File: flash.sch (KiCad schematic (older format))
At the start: 13 parts, among them J1 USB_B_Micro, Q1 PN2222A, Q2 PN2222A, U1 CP2102N-A01-GQFN24

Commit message: Add first iteration of PCB design
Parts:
- added J2: Conn_01x05, Pin_Headers:Pin_Header_Straight_1x05_Pitch2.54mm, symbol Connector_Generic:Conn_01x05
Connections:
- net EN: now also J2.1 (Pin_1)
- net GND: now also J2.5 (Pin_5)
- net GPIO0: now also J2.4 (Pin_4)
- net RX: now also J2.3 (Pin_3)
- net TX: now also J2.2 (Pin_2)
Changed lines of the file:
@@
 Wire Wire Line
 	7800 3700 8300 3700
+$Comp
+L Connector_Generic:Conn_01x05 J2
+U 1 1 5CD3182A
+P 9750 2650
+F 0 "J2" H 9830 2692 50  0000 L CNN
+F 1 "Conn_01x05" H 9830 2601 50  0000 L CNN
+F 2 "Pin_Headers:Pin_Header_Straight_1x05_Pitch2.54mm" H 9750 2650 50  0001 C CNN
+F 3 "~" H 9750 2650 50  0001 C CNN
+	1    9750 2650
+	1    0    0    -1
+$EndComp
+Wire Wire Line
+	9550 2850 9350 2850
+Wire Wire Line
+	9350 2850 9350 3050
+$Comp
+L power:GND #PWR07
+U 1 1 5CD34B89
+P 9350 3050
+F 0 "#PWR07" H 9350 2800 50  0001 C CNN
+F 1 "GND" H 9355 2877 50  0000 C CNN
+F 2 "" H 9350 3050 50  0001 C CNN
+F 3 "" H 9350 3050 50  0001 C CNN
+	1    9350 3050
+	1    0    0    -1
+$EndComp
+Wire Wire Line
+	9550 2750 9350 2750
+Text Label 9350 2750 2    50   ~ 0
+GPIO0
+Wire Wire Line
+	9550 2650 9350 2650
+Text Label 9350 2650 2    50   ~ 0
+RX
+Wire Wire Line
+	9550 2550 9350 2550
+Text Label 9350 2550 2    50   ~ 0
+TX
+Wire Wire Line
+	9550 2450 9350 2450
+Text Label 9350 2450 2    50   ~ 0
+EN
 $EndSCHEMATC

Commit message: Finish PCB
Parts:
- U1: footprint digikey-footprints:QFN-24-1EP_4x4mm -> Housings_DFN_QFN:QFN-24-1EP_4x4mm_Pitch0.5mm
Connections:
- net at R1.1, U1.5 (VIO): now also C1.1, C2.1, U1.6 (VDD)
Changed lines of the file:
@@
 F 0 "U1" H 5800 4581 50  0000 C CNN
 F 1 "CP2102N-A01-GQFN24" H 5800 4490 50  0000 C CNN
-F 2 "digikey-footprints:QFN-24-1EP_4x4mm" H 6250 2700 50  0001 L CNN
+F 2 "Housings_DFN_QFN:QFN-24-1EP_4x4mm_Pitch0.5mm" H 6250 2700 50  0001 L CNN
 F 3 "https://www.silabs.com/documents/public/data-sheets/cp2102n-datasheet.pdf" H 5850 2450 50  0001 C CNN
 	1    5800 3500
@@
 	5800 2600 5800 2150
 Wire Wire Line
-	5800 2150 5500 2150
+	5800 2150 5700 2150
 Wire Wire Line
 	7800 2450 8300 2450
@@
 Text Label 9350 2450 2    50   ~ 0
 EN
+Wire Wire Line
+	5700 2400 5700 2150
+Connection ~ 5700 2400
+Connection ~ 5700 2150
+Wire Wire Line
+	5700 2150 5500 2150
 $EndSCHEMATC

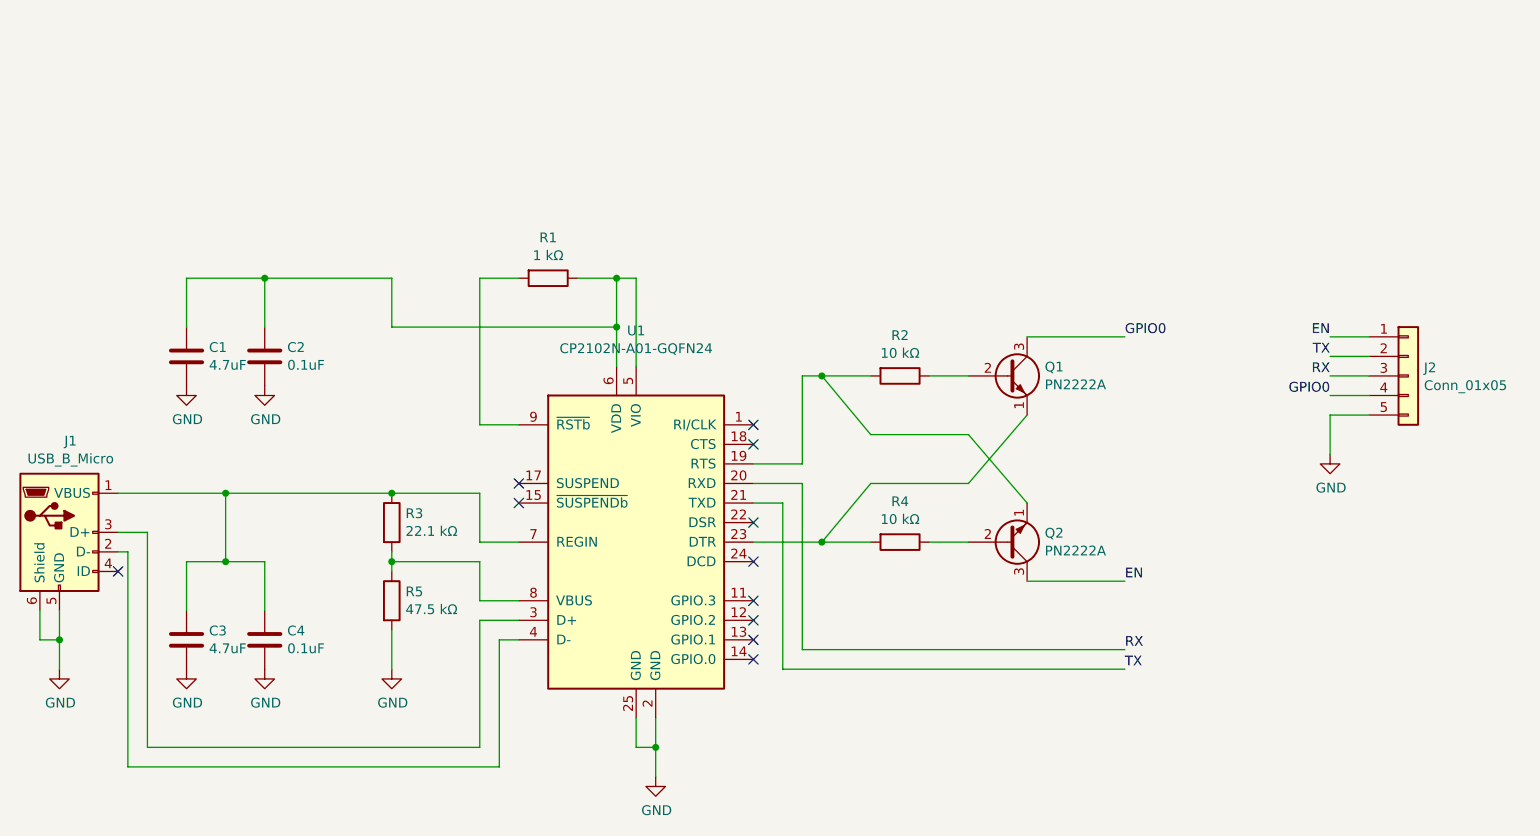
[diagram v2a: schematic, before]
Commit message: Swap RX/TX pins, fix DTR/RTS transistor wiring
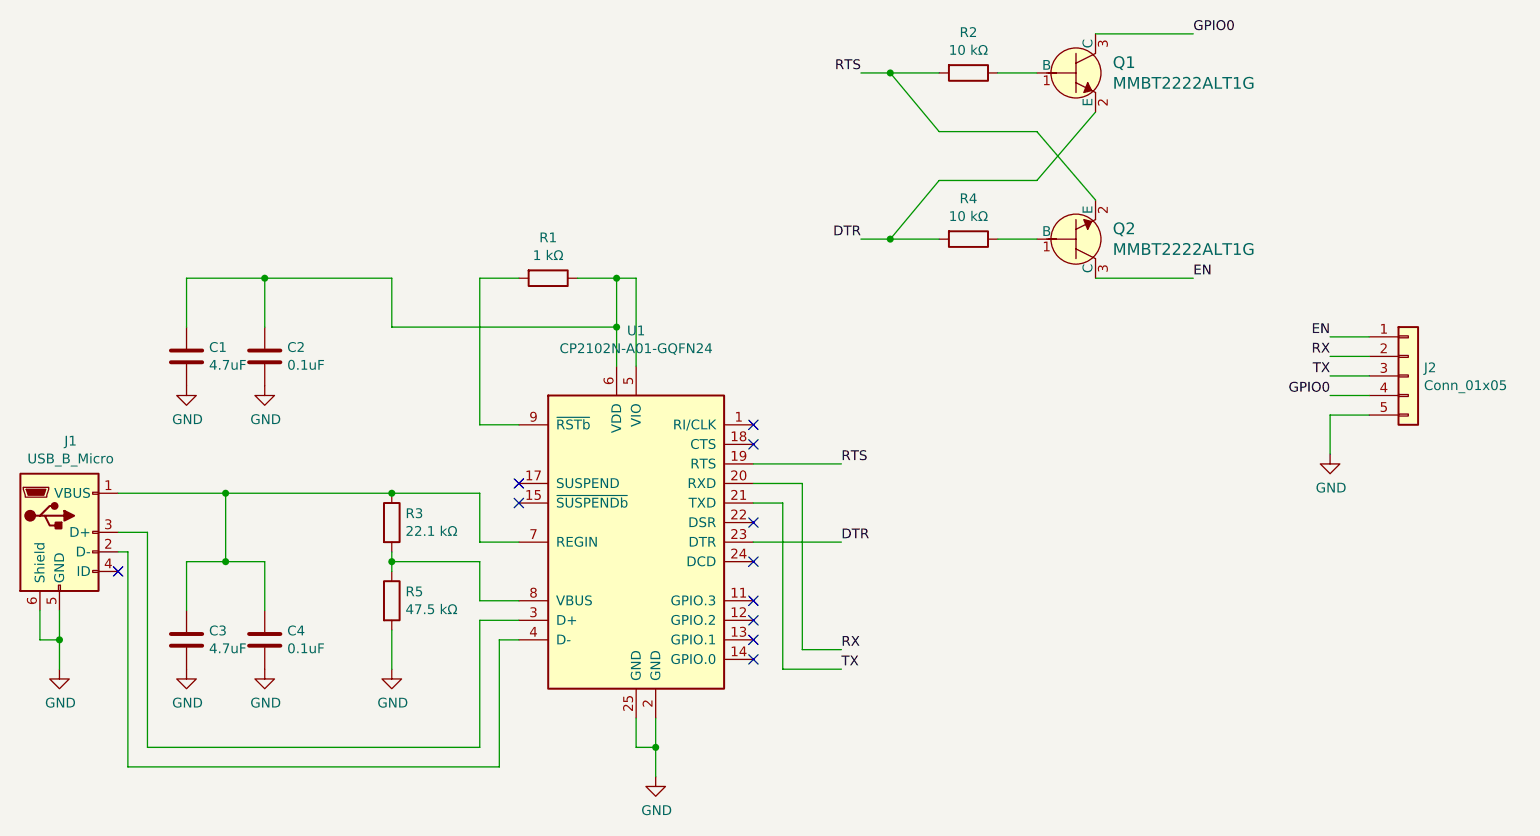
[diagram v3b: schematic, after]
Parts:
- removed Q1, Q2: PN2222A, mmbt2222alt1g:mmbt2222alt1g, symbol Transistor_BJT:PN2222A
- added Q1, Q2: MMBT2222ALT1G, mmbt2222alt1g:mmbt2222alt1g, symbol dk_Transistors-Bipolar-BJT-Single:MMBT2222ALT1G
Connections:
- net EN: now also Q2.3 (C)
- net GPIO0: now also Q1.3 (C)
- net RX: now also J2.2 (Pin_2); no longer J2.3 (Pin_3)
- net TX: now also J2.3 (Pin_3); no longer J2.2 (Pin_2)
- net RTS: now reaches R2.2, U1.19 (RTS)
- net RTS: now also Q2.2 (E)
- net DTR: now reaches R4.2, U1.23 (DTR)
- net DTR: now also Q1.2 (E)
- net at R4.1: now also Q2.1 (B)
- net at R2.1: now also Q1.1 (B)
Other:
- moved on the sheet: R2, R4
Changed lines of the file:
@@
 L Device:R R4
 U 1 1 5CD352C9
-P 7150 3500
-F 0 "R4" V 6943 3500 50  0000 C CNN
-F 1 "10 kΩ" V 7034 3500 50  0000 C CNN
-F 2 "Resistors_SMD:R_0603_HandSoldering" V 7080 3500 50  0001 C CNN
-F 3 "~" H 7150 3500 50  0001 C CNN
-	1    7150 3500
+P 7500 1950
+F 0 "R4" V 7293 1950 50  0000 C CNN
+F 1 "10 kΩ" V 7384 1950 50  0000 C CNN
+F 2 "Resistors_SMD:R_0603_HandSoldering" V 7430 1950 50  0001 C CNN
+F 3 "~" H 7500 1950 50  0001 C CNN
+	1    7500 1950
 	0    1    1    0
 $EndComp
-$Comp
-L Transistor_BJT:PN2222A Q2
-U 1 1 5CD37793
-P 7700 3500
-F 0 "Q2" H 7890 3454 50  0000 L CNN
-F 1 "PN2222A" H 7890 3545 50  0000 L CNN
-F 2 "mmbt2222alt1g:mmbt2222alt1g" H 7900 3425 50  0001 L CIN
-F 3 "http://www.fairchildsemi.com/ds/PN/PN2222A.pdf" H 7700 3500 50  0001 L CNN
-	1    7700 3500
-	1    0    0    1
-$EndComp
-Wire Wire Line
-	7300 3500 7500 3500
+Wire Wire Line
+	7650 1950 7850 1950
 $Comp
 L Device:R R2
 U 1 1 5CD3C513
-P 7150 2650
-F 0 "R2" V 6943 2650 50  0000 C CNN
-F 1 "10 kΩ" V 7034 2650 50  0000 C CNN
-F 2 "Resistors_SMD:R_0603_HandSoldering" V 7080 2650 50  0001 C CNN
-F 3 "~" H 7150 2650 50  0001 C CNN
-	1    7150 2650
+P 7500 1100
+F 0 "R2" V 7293 1100 50  0000 C CNN
+F 1 "10 kΩ" V 7384 1100 50  0000 C CNN
+F 2 "Resistors_SMD:R_0603_HandSoldering" V 7430 1100 50  0001 C CNN
+F 3 "~" H 7500 1100 50  0001 C CNN
+	1    7500 1100
 	0    1    1    0
 $EndComp
-Text Label 8300 3700 0    50   ~ 0
+Text Label 8650 2150 0    50   ~ 0
 EN
-Text Label 8300 2450 0    50   ~ 0
+Text Label 8650 900  0    50   ~ 0
 GPIO0
 Wire Wire Line
 	6550 3300 6550 4150
-Wire Wire Line
-	6550 4150 8300 4150
-Text Label 8300 4150 0    50   ~ 0
+Text Label 6850 4150 0    50   ~ 0
 TX
-$Comp
-L Transistor_BJT:PN2222A Q1
-U 1 1 5CD387D0
-P 7700 2650
-F 0 "Q1" H 7890 2696 50  0000 L CNN
-F 1 "PN2222A" H 7890 2605 50  0000 L CNN
-F 2 "mmbt2222alt1g:mmbt2222alt1g" H 7900 2575 50  0001 L CIN
-F 3 "http://www.fairchildsemi.com/ds/PN/PN2222A.pdf" H 7700 2650 50  0001 L CNN
-	1    7700 2650
-	1    0    0    -1
-$EndComp
-Wire Wire Line
-	7300 2650 7500 2650
-Wire Wire Line
-	6400 3500 6750 3500
-Wire Wire Line
-	6750 3500 7000 3200
-Connection ~ 6750 3500
-Wire Wire Line
-	6750 3500 7000 3500
-Wire Wire Line
-	6750 2650 7000 2650
-Wire Wire Line
-	6750 2650 7000 2950
-Wire Wire Line
-	6400 3100 6650 3100
-Wire Wire Line
-	6650 3100 6650 2650
-Wire Wire Line
-	6650 2650 6750 2650
-Connection ~ 6750 2650
-Wire Wire Line
-	7800 2850 7500 3200
-Wire Wire Line
-	7500 3200 7000 3200
-Wire Wire Line
-	7000 2950 7500 2950
-Wire Wire Line
-	7500 2950 7800 3300
+Wire Wire Line
+	7650 1100 7850 1100
+Wire Wire Line
+	7100 1950 7350 1650
+Wire Wire Line
+	7100 1950 7350 1950
+Wire Wire Line
+	7100 1100 7350 1100
+Wire Wire Line
+	7100 1100 7350 1400
+Wire Wire Line
+	8150 1300 7850 1650
+Wire Wire Line
+	7850 1650 7350 1650
+Wire Wire Line
+	7350 1400 7850 1400
+Wire Wire Line
+	7850 1400 8150 1750
 Wire Wire Line
 	5200 3800 5000 3800
@@
 	5800 2150 5700 2150
 Wire Wire Line
-	7800 2450 8300 2450
+	8150 900  8650 900
 Wire Wire Line
 	6400 3200 6650 3200
 Wire Wire Line
 	6650 3200 6650 4050
-Text Label 8300 4050 0    50   ~ 0
+Text Label 6850 4050 0    50   ~ 0
 RX
 Wire Wire Line
-	6650 4050 8300 4050
-Wire Wire Line
-	7800 3700 8300 3700
+	8150 2150 8650 2150
 $Comp
 L Connector_Generic:Conn_01x05 J2
@@
 Wire Wire Line
 	9550 2650 9350 2650
+Text Label 9350 2550 2    50   ~ 0
+RX
+Wire Wire Line
+	9550 2550 9350 2550
 Text Label 9350 2650 2    50   ~ 0
-RX
-Wire Wire Line
-	9550 2550 9350 2550
-Text Label 9350 2550 2    50   ~ 0
 TX
 Wire Wire Line
@@
 Wire Wire Line
 	5700 2150 5500 2150
+Text Label 6850 3100 0    50   ~ 0
+RTS
+Wire Wire Line
+	6400 3500 6850 3500
+Text Label 6850 3500 0    50   ~ 0
+DTR
+Wire Wire Line
+	6400 3100 6850 3100
+Wire Wire Line
+	7100 1950 6950 1950
+Connection ~ 7100 1950
+Wire Wire Line
+	7100 1100 6950 1100
+Connection ~ 7100 1100
+Text Label 6950 1100 2    50   ~ 0
+RTS
+Text Label 6950 1950 2    50   ~ 0
+DTR
+Wire Wire Line
+	6650 4050 6850 4050
+Wire Wire Line
+	6550 4150 6850 4150
+$Comp
+L dk_Transistors-Bipolar-BJT-Single:MMBT2222ALT1G Q1
+U 1 1 5CFDD0F3
+P 8050 1100
+F 0 "Q1" H 8238 1153 60  0000 L CNN
+F 1 "MMBT2222ALT1G" H 8238 1047 60  0000 L CNN
+F 2 "mmbt2222alt1g:mmbt2222alt1g" H 8250 1300 60  0001 L CNN
+F 3 "http://www.onsemi.com/pub/Collateral/MMBT2222LT1-D.PDF" H 8250 1400 60  0001 L CNN
+F 4 "MMBT2222ALT1GOSCT-ND" H 8250 1500 60  0001 L CNN "Digi-Key_PN"
+F 5 "MMBT2222ALT1G" H 8250 1600 60  0001 L CNN "MPN"
+F 6 "Discrete Semiconductor Products" H 8250 1700 60  0001 L CNN "Category"
+F 7 "Transistors - Bipolar (BJT) - Single" H 8250 1800 60  0001 L CNN "Family"
+F 8 "http://www.onsemi.com/pub/Collateral/MMBT2222LT1-D.PDF" H 8250 1900 60  0001 L CNN "DK_Datasheet_Link"
+F 9 "/product-detail/en/on-semiconductor/MMBT2222ALT1G/MMBT2222ALT1GOSCT-ND/1139806" H 8250 2000 60  0001 L CNN "DK_Detail_Page"
+F 10 "TRANS NPN 40V 0.6A SOT23" H 8250 2100 60  0001 L CNN "Description"
+F 11 "ON Semiconductor" H 8250 2200 60  0001 L CNN "Manufacturer"
+F 12 "Active" H 8250 2300 60  0001 L CNN "Status"
+	1    8050 1100
+	1    0    0    -1
+$EndComp
+$Comp
+L dk_Transistors-Bipolar-BJT-Single:MMBT2222ALT1G Q2
+U 1 1 5CFEB52D
+P 8050 1950
+F 0 "Q2" H 8238 1897 60  0000 L CNN
+F 1 "MMBT2222ALT1G" H 8238 2003 60  0000 L CNN
+F 2 "mmbt2222alt1g:mmbt2222alt1g" H 8250 2150 60  0001 L CNN
+F 3 "http://www.onsemi.com/pub/Collateral/MMBT2222LT1-D.PDF" H 8250 2250 60  0001 L CNN
+F 4 "MMBT2222ALT1GOSCT-ND" H 8250 2350 60  0001 L CNN "Digi-Key_PN"
+F 5 "MMBT2222ALT1G" H 8250 2450 60  0001 L CNN "MPN"
+F 6 "Discrete Semiconductor Products" H 8250 2550 60  0001 L CNN "Category"
+F 7 "Transistors - Bipolar (BJT) - Single" H 8250 2650 60  0001 L CNN "Family"
+F 8 "http://www.onsemi.com/pub/Collateral/MMBT2222LT1-D.PDF" H 8250 2750 60  0001 L CNN "DK_Datasheet_Link"
+F 9 "/product-detail/en/on-semiconductor/MMBT2222ALT1G/MMBT2222ALT1GOSCT-ND/1139806" H 8250 2850 60  0001 L CNN "DK_Detail_Page"
+F 10 "TRANS NPN 40V 0.6A SOT23" H 8250 2950 60  0001 L CNN "Description"
+F 11 "ON Semiconductor" H 8250 3050 60  0001 L CNN "Manufacturer"
+F 12 "Active" H 8250 3150 60  0001 L CNN "Status"
+	1    8050 1950
+	1    0    0    1
+$EndComp
 $EndSCHEMATC
